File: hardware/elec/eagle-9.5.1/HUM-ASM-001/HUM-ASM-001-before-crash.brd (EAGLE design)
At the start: 99.1 x 99.1 mm, 61 parts, among them J1 B2B-XH-AM(LF)(SN), J2 75869-131LF, J22 75869-131LF, J23 75869-131LF, K1 7-1393239-7, K2 7-1393239-7, Q1 IRLB8721PBF, Q2 IRLB8721PBF, U1 MCP23017-E/SP

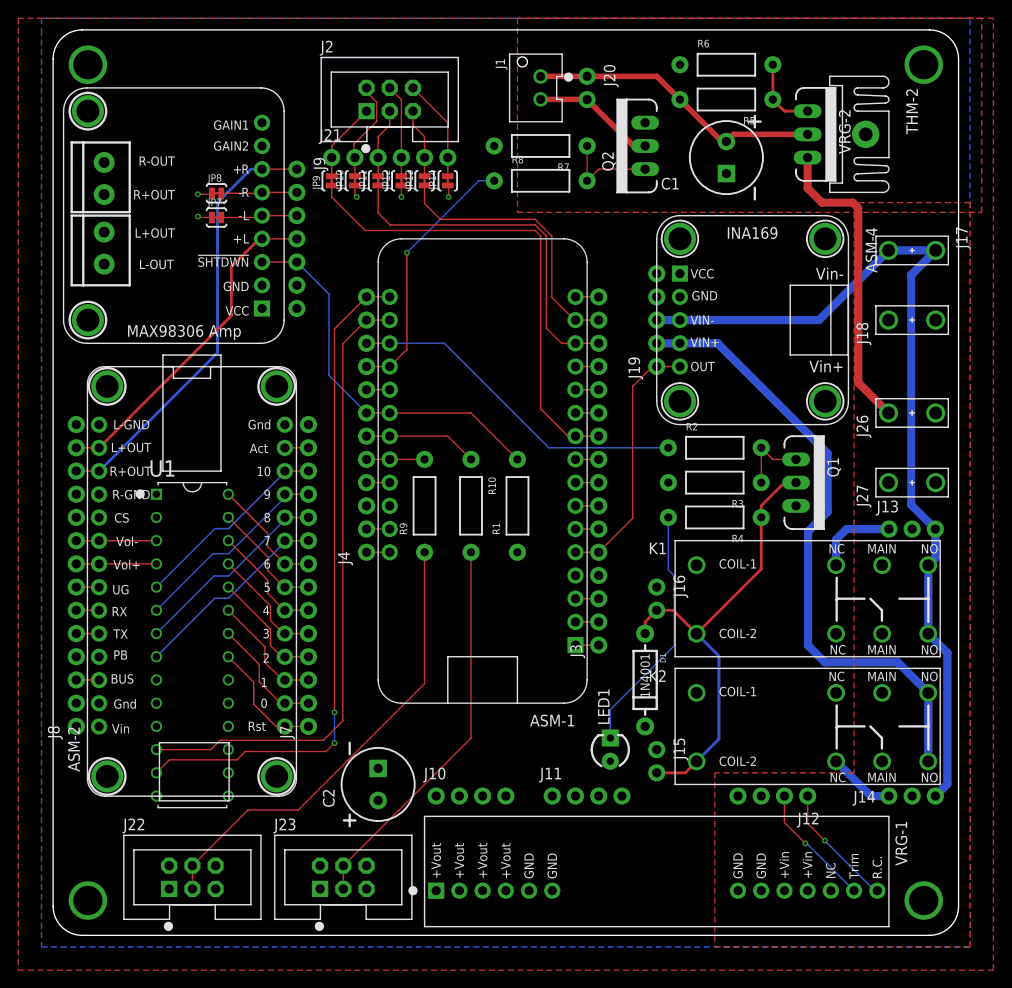
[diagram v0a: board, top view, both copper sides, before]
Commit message: * Fixed crash / recovery inconsistency * Pre silk screen clean up
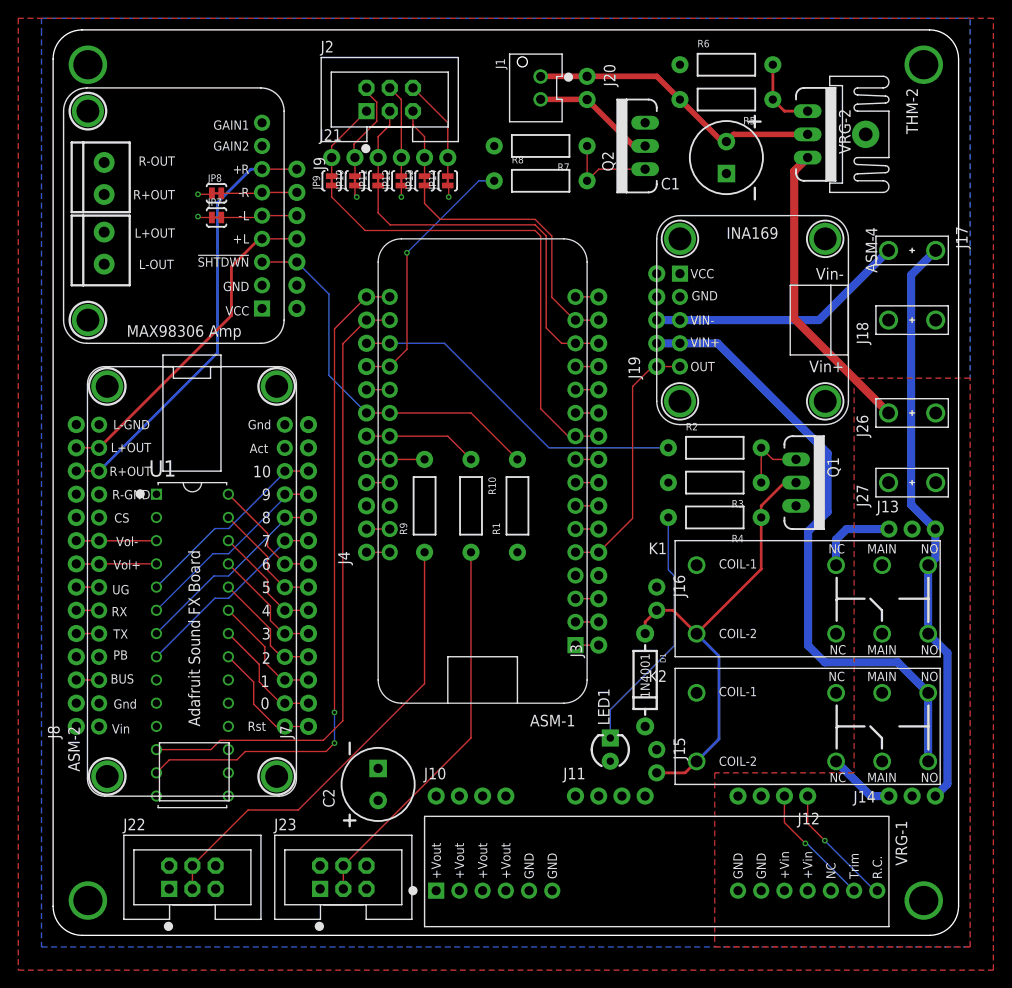
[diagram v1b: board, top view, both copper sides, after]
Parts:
- moved J11 2.54 mm to (57.1, 15.2)
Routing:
- net MIST-VIN: track 97.3 -> 92.2 mm
- net N$26: track 2.59 -> 0.00 mm
- net 48V: track 33.6 -> 32.8 mm
- removed copper zone on layer 1, net 24V-CUTOUT
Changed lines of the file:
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@@
 <attribute name="VALUE" x="40.64" y="12.065" size="1.27" layer="27"/>
 </element>
-<element name="J11" library="MG-Eagle_v1" package="1X04_NO_SILK_ALL_ROUND" value="" x="54.61" y="15.24" smashed="yes">
-<attribute name="NAME" x="53.2638" y="17.0688" size="1.27" layer="25" ratio="10"/>
-<attribute name="PROD_ID" value="CONN-09696" x="170.18" y="-137.16" size="1.778" layer="27" display="off"/>
-<attribute name="VALUE" x="53.34" y="12.065" size="1.27" layer="27"/>
+<element name="J11" library="MG-Eagle_v1" package="1X04_NO_SILK_ALL_ROUND" value="" x="57.15" y="15.24" smashed="yes">
+<attribute name="NAME" x="55.8038" y="17.0688" size="1.27" layer="25" ratio="10"/>
+<attribute name="PROD_ID" value="CONN-09696" x="172.72" y="-137.16" size="1.778" layer="27" display="off"/>
+<attribute name="VALUE" x="55.88" y="12.065" size="1.27" layer="27"/>
 </element>
 <element name="J12" library="MG-Eagle_v1" package="1X04_NO_SILK_ALL_ROUND" value="" x="82.55" y="15.24" smashed="yes" rot="R180">
@@
 <wire x1="17.3736" y1="78.5368" x2="15.9512" y2="78.5368" width="0.1524" layer="1"/>
 <wire x1="15.9512" y1="78.5368" x2="15.8496" y2="78.6384" width="0.1524" layer="1"/>
-<wire x1="91.4019" y1="49.53" x2="96.5581" y2="49.53" width="0" layer="19" extent="1-1"/>
 </signal>
 <signal name="5V">
@@
 <contactref element="J26" pad="2"/>
 <polygon width="0.3048" layer="1" isolate="0.8128">
-<vertex x="100.33" y="80.1624"/>
-<vertex x="87.63" y="80.1624"/>
+<vertex x="100.33" y="60.96"/>
+<vertex x="87.63" y="60.96"/>
 <vertex x="87.63" y="17.78"/>
 <vertex x="72.39" y="17.78"/>
@@
 <vertex x="100.33" y="-1.27"/>
 </polygon>
-<wire x1="91.4019" y1="57.15" x2="88.0872" y2="60.4647" width="0.889" layer="1"/>
-<wire x1="87.4776" y1="80.1624" x2="84.1248" y2="80.1624" width="0.889" layer="1"/>
-<wire x1="84.1248" y1="80.1624" x2="82.55" y2="81.7372" width="0.889" layer="1"/>
-<wire x1="82.55" y1="81.7372" x2="82.55" y2="85.09" width="0.889" layer="1"/>
-<wire x1="88.0872" y1="60.4647" x2="88.0872" y2="79.5528" width="0.889" layer="1"/>
-<wire x1="88.0872" y1="79.5528" x2="87.4776" y2="80.1624" width="0.889" layer="1"/>
+<wire x1="91.4019" y1="57.15" x2="81.0768" y2="67.4751" width="0.889" layer="1"/>
+<wire x1="81.0768" y1="83.6168" x2="82.55" y2="85.09" width="0.889" layer="1"/>
+<wire x1="81.0768" y1="67.4751" x2="81.0768" y2="83.6168" width="0.889" layer="1"/>
 </signal>
 <signal name="N$27">
@@
 <wire x1="97.8408" y1="30.8992" x2="95.74" y2="33" width="0.889" layer="16"/>
 <wire x1="97.8408" y1="16.5608" x2="97.8408" y2="30.8992" width="0.889" layer="16"/>
-<wire x1="91.4019" y1="74.93" x2="96.5581" y2="74.93" width="0.889" layer="16"/>
+<wire x1="96.5581" y1="74.93" x2="91.4019" y2="74.93" width="0" layer="19" extent="1-1"/>
 </signal>
 <signal name="N$16">
@@
 <contactref element="ASM-2" pad="13"/>
 <contactref element="J7" pad="13"/>
-<wire x1="25.351" y1="53.327" x2="25.364" y2="53.34" width="0.1524" layer="1"/>
-<wire x1="25.364" y1="53.34" x2="27.94" y2="53.34" width="0.1524" layer="1"/>
+<wire x1="25.351" y1="53.327" x2="27.94" y2="53.34" width="0" layer="19" extent="1-1"/>
 </signal>
 <signal name="USB/VBUS">
@@
 <wire x1="22.7584" y1="81.1784" x2="22.86" y2="81.28" width="0.1524" layer="1"/>
 </signal>
-<signal name="24V-CUTOUT">
-<polygon width="0.3048" layer="1" pour="cutout" isolate="0.3048" rank="2">
-<vertex x="50.8" y="100.33"/>
-<vertex x="50.8" y="79.0956"/>
-<vertex x="101.6" y="79.0956"/>
-<vertex x="101.6" y="100.33"/>
-</polygon>
-</signal>
 </signals>
